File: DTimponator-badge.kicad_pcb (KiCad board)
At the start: 2 copper layers, 71 x 99.5 mm, 29 parts, among them J1 AVR-ISP, SW1 SW_SPDT, SW2 SW_Push, SW3 SW_Push, U1 ATtiny84A-PU

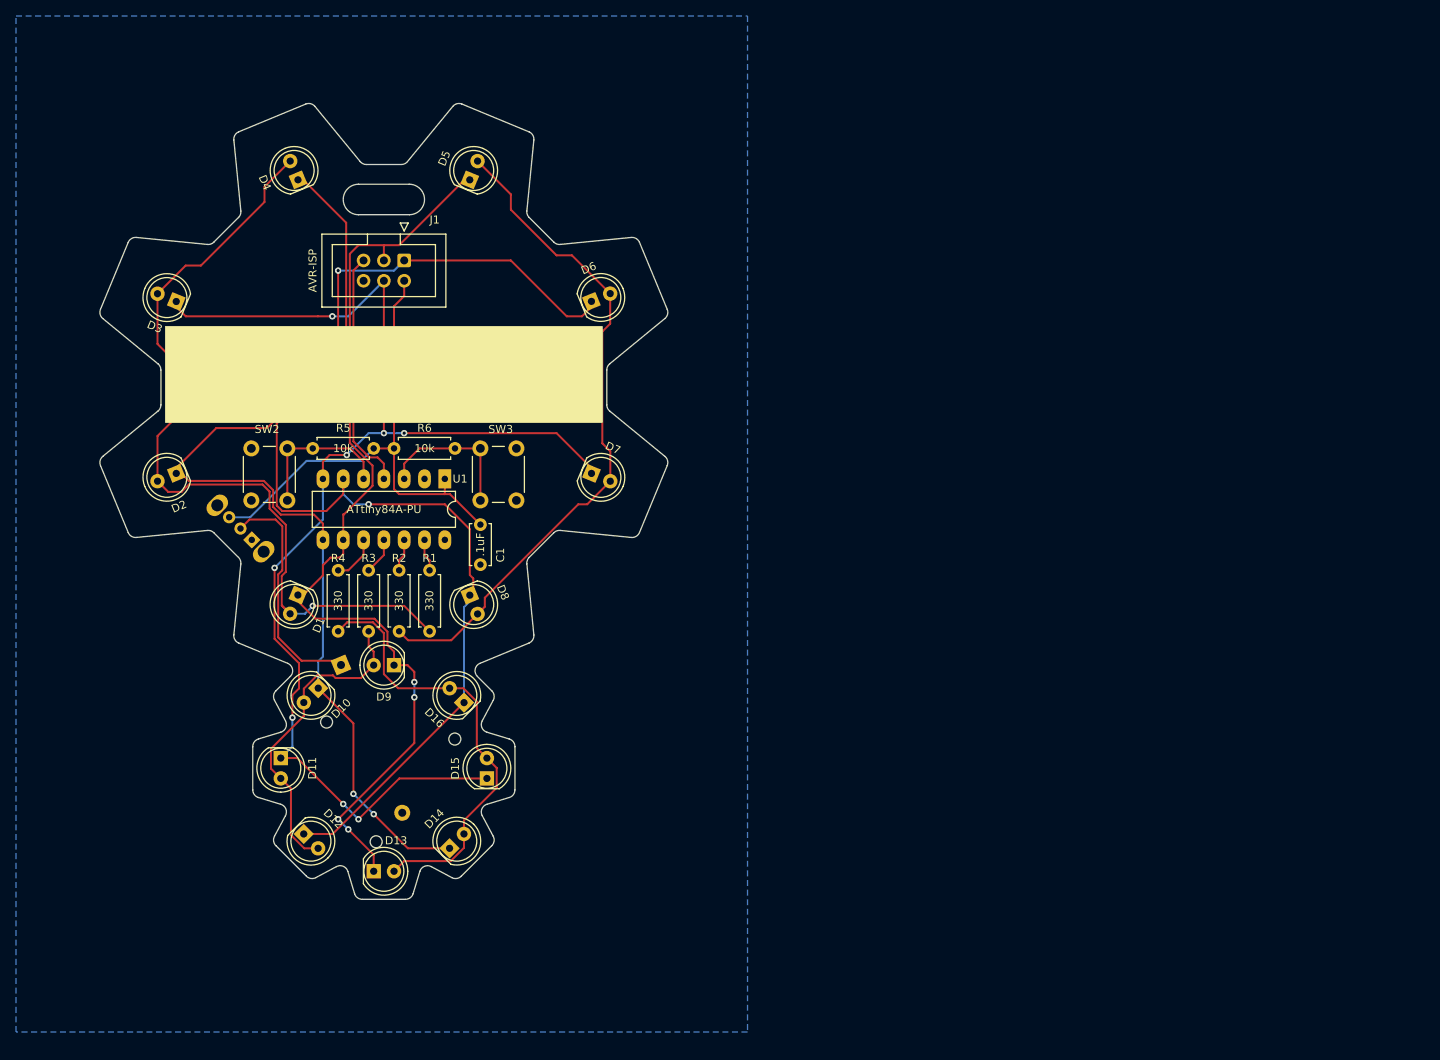
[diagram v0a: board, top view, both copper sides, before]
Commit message: Changed to dimmable SMD LEDs
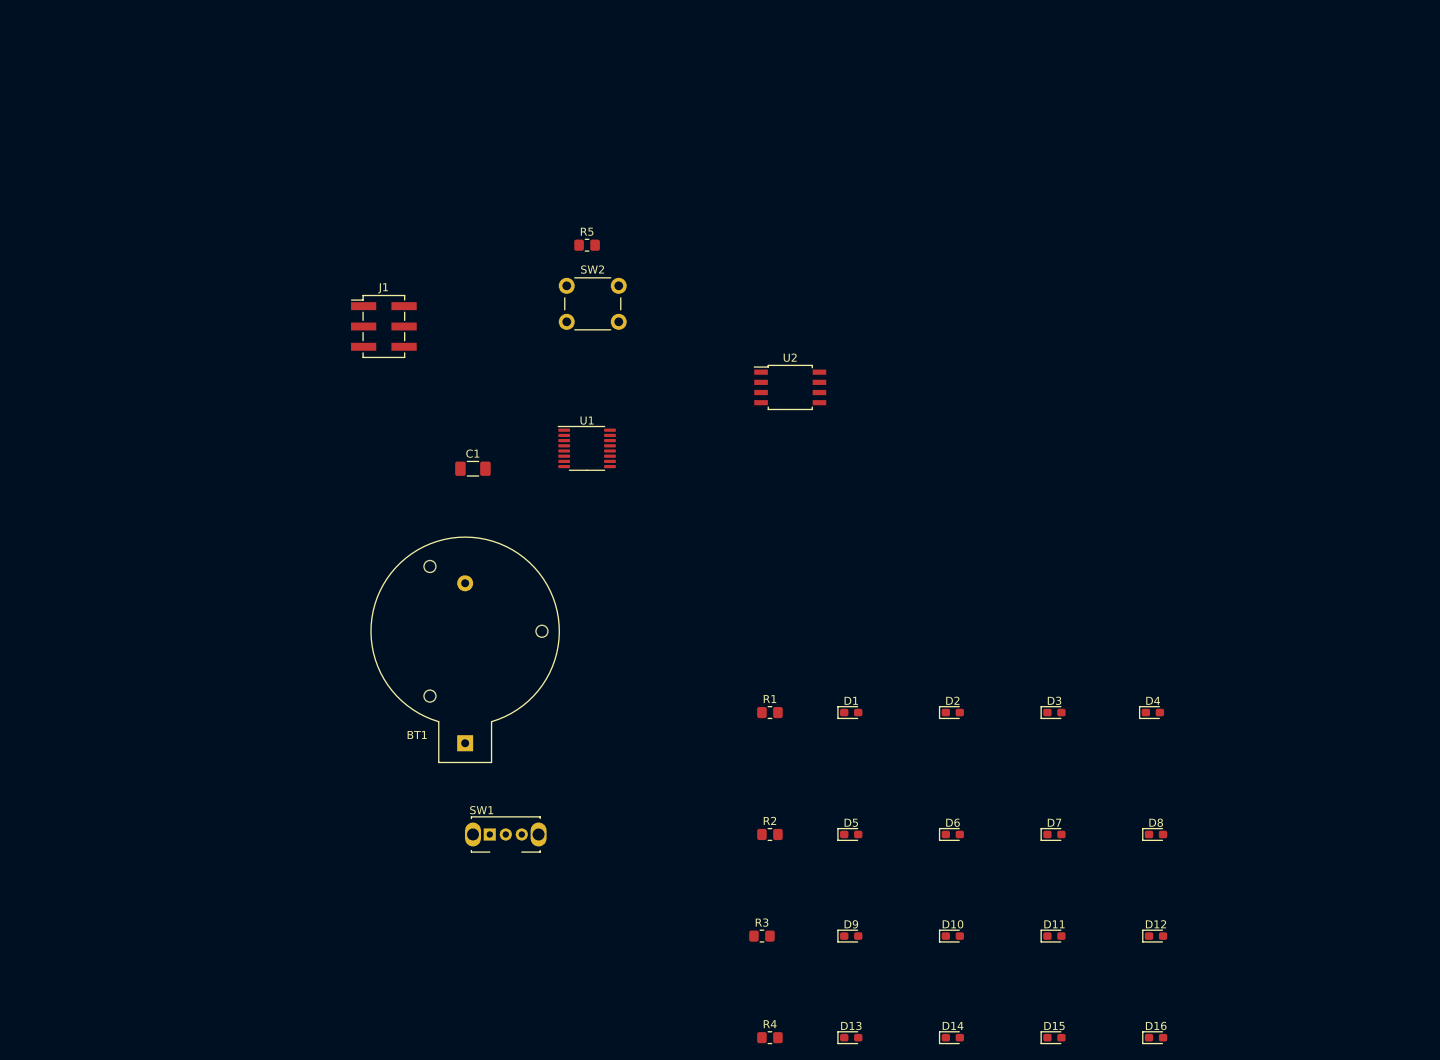
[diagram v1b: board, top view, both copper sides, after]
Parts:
- removed R6: 10k, Resistor_THT:R_Axial_DIN0207_L6.3mm_D2.5mm_P7.62mm_Horizontal
- removed SW3: SW_Push, Button_Switch_THT:SW_PUSH_6mm_H5mm
- added U2: ATtiny85-20S, Package_SO:SOIC-8W_5.3x5.3mm_P1.27mm, F.Cu at (127.0, 76.2)
- BT1: footprint CogLightBadgeTHT:MP000362_CR2032_Holder_THT -> DTimponator-badge:MP000362_CR2032_Holder_THT; moved to F.Cu
- C1: footprint Capacitor_THT:C_Disc_D5.0mm_W2.5mm_P5.00mm -> Capacitor_SMD:C_1206_3216Metric_Pad1.33x1.80mm_HandSolder
- D1, D10, D11, D12, D13, D14, D15, D16, D2, D3, D4, D5, D6, D7, D8, D9: footprint LED_THT:LED_D5.0mm -> LED_SMD:LED_0603_1608Metric_Pad1.05x0.95mm_HandSolder
- J1: footprint Connector_IDC:IDC-Header_2x03_P2.54mm_Vertical -> Connector_PinHeader_2.54mm:PinHeader_2x03_P2.54mm_Vertical_SMD
- R1, R2, R3, R4: value 330 -> R; footprint Resistor_THT:R_Axial_DIN0207_L6.3mm_D2.5mm_P7.62mm_Horizontal -> Resistor_SMD:R_0805_2012Metric_Pad1.20x1.40mm_HandSolder
- R5: footprint Resistor_THT:R_Axial_DIN0207_L6.3mm_D2.5mm_P7.62mm_Horizontal -> Resistor_SMD:R_0805_2012Metric_Pad1.20x1.40mm_HandSolder
- SW1: footprint CogLightBadgeTHT:OS102011MA1QN1_SPDT_SlideSwithch_THT -> DTimponator-badge:OS102011MA1QN1_SPDT_SlideSwithch_THT; moved to F.Cu
- U1: value ATtiny84A-PU -> 74HC595; footprint Package_DIP:DIP-14_W7.62mm_LongPads -> Package_SO:TSSOP-16_4.4x5mm_P0.65mm
- moved D4 125.9 mm to (172.3, 116.8), turned to 0 degrees
- moved D3 121.2 mm to (160.0, 116.8), turned to 0 degrees
- moved D12 107.3 mm to (172.7, 144.8), turned to 0 degrees
- moved D2 101.6 mm to (147.3, 116.8), turned to 0 degrees
- moved D11 99.2 mm to (160.0, 144.8), turned to 0 degrees
- moved D16 96.1 mm to (172.7, 157.5), turned to 0 degrees
- moved D5 94.7 mm to (134.6, 132.1), turned to 0 degrees
- moved D8 90.8 mm to (172.7, 132.1), turned to 0 degrees
- moved D10 85.2 mm to (147.3, 144.8), turned to 0 degrees
- moved D6 80.5 mm to (147.3, 132.1), turned to 0 degrees
- moved D15 78.0 mm to (160.0, 157.5), turned to 0 degrees
- moved R4 74.1 mm to (124.5, 157.5), turned to 0 degrees
- moved D7 73.4 mm to (160.0, 132.1), turned to 0 degrees
- moved D1 70.7 mm to (134.6, 116.8), turned to 0 degrees
- moved D14 67.2 mm to (147.3, 157.5), turned to 0 degrees
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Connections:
- D1 pad 1: /sink1 -> Net-(D1-Pad1)
- D10 pad 1: /sink2 -> Net-(D10-Pad1)
- D11 pad 1: /sink3 -> Net-(D10-Pad1)
- D11 pad 2: Net-(D10-Pad2) -> Net-(D11-Pad2)
- D12 pad 1: /sink4 -> Net-(D10-Pad1)
- D12 pad 2: Net-(D10-Pad2) -> Net-(D12-Pad2)
- D13 pad 1: /sink1 -> Net-(D13-Pad1)
- D13 pad 2: Net-(D13-Pad2) -> Net-(D1-Pad2)
- D14 pad 1: /sink2 -> Net-(D13-Pad1)
- D14 pad 2: Net-(D13-Pad2) -> Net-(D10-Pad2)
- D15 pad 1: /sink3 -> Net-(D13-Pad1)
- D15 pad 2: Net-(D13-Pad2) -> Net-(D11-Pad2)
- D16 pad 1: /sink4 -> Net-(D13-Pad1)
- D16 pad 2: Net-(D13-Pad2) -> Net-(D12-Pad2)
- D2 pad 1: /sink2 -> Net-(D1-Pad1)
- D2 pad 2: Net-(D1-Pad2) -> Net-(D10-Pad2)
- D3 pad 1: /sink3 -> Net-(D1-Pad1)
- D3 pad 2: Net-(D1-Pad2) -> Net-(D11-Pad2)
- D4 pad 1: /sink4 -> Net-(D1-Pad1)
- D4 pad 2: Net-(D1-Pad2) -> Net-(D12-Pad2)
- D5 pad 1: /sink1 -> Net-(D5-Pad1)
- D5 pad 2: Net-(D5-Pad2) -> Net-(D1-Pad2)
- D6 pad 1: /sink2 -> Net-(D5-Pad1)
- D6 pad 2: Net-(D5-Pad2) -> Net-(D10-Pad2)
- D7 pad 1: /sink3 -> Net-(D5-Pad1)
- D7 pad 2: Net-(D5-Pad2) -> Net-(D11-Pad2)
- D8 pad 1: /sink4 -> Net-(D5-Pad1)
- D8 pad 2: Net-(D5-Pad2) -> Net-(D12-Pad2)
- D9 pad 1: /sink1 -> Net-(D10-Pad1)
- D9 pad 2: Net-(D10-Pad2) -> Net-(D1-Pad2)
- J1 pad 1: /sink2 -> /MISO
- J1 pad 3: /sink1 -> /SCK
- J1 pad 4: /sink3 -> /MOSI
- J1 pad 5: Net-(J1-Pad5) -> /~{RST}
- R1 pad 1: Net-(D1-Pad2) -> Net-(D1-Pad1)
- R1 pad 2: /source1 -> Net-(R1-Pad2)
- R2 pad 1: Net-(D5-Pad2) -> Net-(D5-Pad1)
- R2 pad 2: /source2 -> Net-(R2-Pad2)
- R3 pad 1: Net-(D10-Pad2) -> Net-(D10-Pad1)
- R3 pad 2: /source3 -> Net-(R3-Pad2)
- R4 pad 1: Net-(D13-Pad2) -> Net-(D13-Pad1)
- R4 pad 2: /source4 -> Net-(R4-Pad2)
- R5 pad 2: Net-(R5-Pad2) -> /MOSI
- SW1 pad 1: Net-(SW1-Pad1) -> unconnected-(SW1-Pad1)
- SW2 pad 1: Net-(R5-Pad2) -> /MOSI
- U1 pad 1: VCC -> Net-(D1-Pad1)
- U1 pad 10: /source4 -> VCC
- U1 pad 11: /source3 -> /SCK
- U1 pad 12: /source2 -> /MISO
- U1 pad 13: /source1 -> /~{OE}_PWM
- U1 pad 14: GND -> /SER
- U1 pad 2: Net-(U1-Pad2) -> Net-(D1-Pad1)
- U1 pad 3: Net-(R6-Pad2) -> Net-(D1-Pad1)
- U1 pad 4: Net-(J1-Pad5) -> Net-(R1-Pad2)
- U1 pad 5: Net-(R5-Pad2) -> Net-(R2-Pad2)
- U1 pad 6: /sink4 -> Net-(R3-Pad2)
- U1 pad 7: /sink3 -> Net-(R4-Pad2)
- U1 pad 8: /sink2 -> GND
- U1 pad 9: /sink1 -> unconnected-(U1-Pad9)
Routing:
- net /sink3: track 160.6 -> 0.00 mm, vias 8 -> 0
- net /sink2: track 146.6 -> 0.00 mm, vias 3 -> 0
- net /sink4: track 127.3 -> 0.00 mm, vias 1 -> 0
- net /sink1: track 121.2 -> 0.00 mm, vias 4 -> 0
- net Net-(D1-Pad2): track 102.0 -> 0.00 mm, vias 1 -> 0
- net Net-(D5-Pad2): track 84.6 -> 0.00 mm
- net VCC: track 65.3 -> 0.00 mm
- net Net-(D13-Pad2): track 55.9 -> 0.00 mm
- net Net-(D10-Pad2): track 39.8 -> 0.00 mm
- net Net-(J1-Pad5): track 30.0 -> 0.00 mm
- net Net-(BT1-Pad1): track 29.4 -> 0.00 mm
- net Net-(R5-Pad2): track 18.9 -> 0.00 mm
- net Net-(R6-Pad2): track 18.7 -> 0.00 mm
- net /source4: track 5.87 -> 0.00 mm
- net /source3: track 4.60 -> 0.00 mm
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- removed copper zone on B.Cu, net GND
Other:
- board outline removed
- net class Default removed

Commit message: Changed from led matrix to led array for increased brightness, routed pcb.
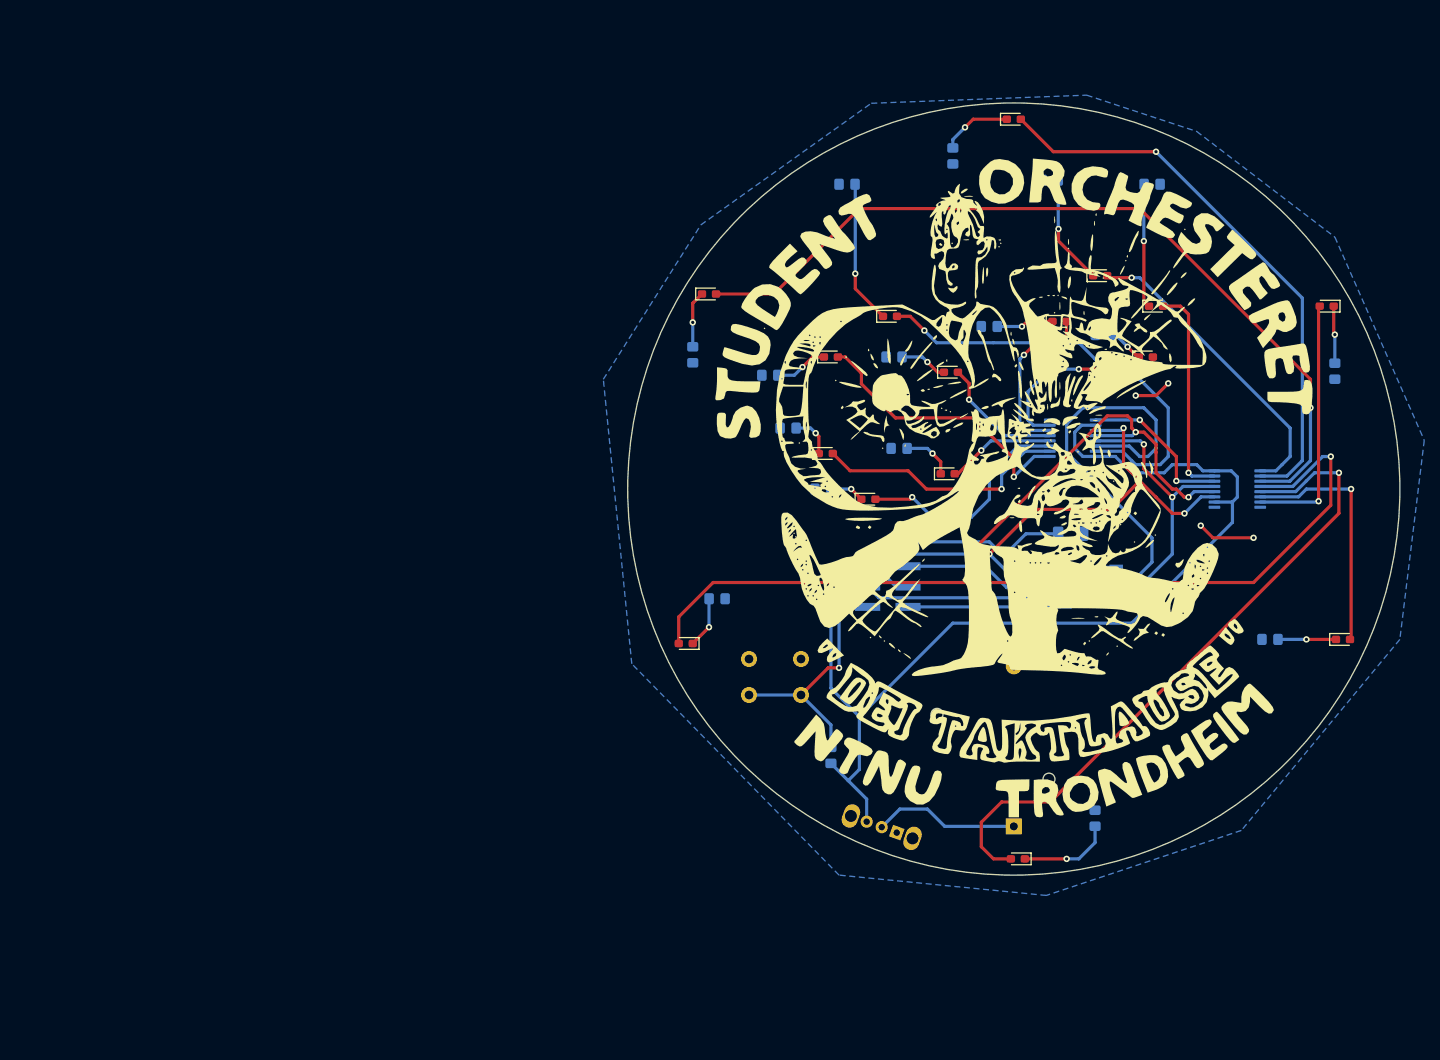
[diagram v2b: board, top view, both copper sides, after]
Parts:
- removed C1: .1uF, Capacitor_SMD:C_1206_3216Metric_Pad1.33x1.80mm_HandSolder
- added C1, 1uF: .1uF, Capacitor_SMD:C_1206_3216Metric_Pad1.33x1.80mm_HandSolder, B.Cu at (162.1, 94.5)
- added G***: LOGO, DTimponator-badge:LOGO, F.Cu at (154.9, 88.9)
- added R10: 220, Resistor_SMD:R_0805_2012Metric_Pad1.20x1.40mm_HandSolder, B.Cu at (172.2, 50.8)
- added R11: 220, Resistor_SMD:R_0805_2012Metric_Pad1.20x1.40mm_HandSolder, B.Cu at (159.5, 50.3)
- added R12: 220, Resistor_SMD:R_0805_2012Metric_Pad1.20x1.40mm_HandSolder, B.Cu at (147.3, 47.3)
- added R13: 220, Resistor_SMD:R_0805_2012Metric_Pad1.20x1.40mm_HandSolder, B.Cu at (114.8, 72.1)
- added R14: 220, Resistor_SMD:R_0805_2012Metric_Pad1.20x1.40mm_HandSolder, B.Cu at (117.9, 102.6)
- added R15: 220, Resistor_SMD:R_0805_2012Metric_Pad1.20x1.40mm_HandSolder, B.Cu at (165.1, 130.0)
- added R16: 220, Resistor_SMD:R_0805_2012Metric_Pad1.20x1.40mm_HandSolder, B.Cu at (187.0, 107.7)
- added R17: 220, Resistor_SMD:R_0805_2012Metric_Pad1.20x1.40mm_HandSolder, B.Cu at (195.1, 74.2)
- added R6: 220, Resistor_SMD:R_0805_2012Metric_Pad1.20x1.40mm_HandSolder, B.Cu at (140.0, 72.4)
- added R7: 220, Resistor_SMD:R_0805_2012Metric_Pad1.20x1.40mm_HandSolder, B.Cu at (151.9, 68.6)
- added R8: 220, Resistor_SMD:R_0805_2012Metric_Pad1.20x1.40mm_HandSolder, B.Cu at (166.1, 69.6)
- added R9, 10k: 10k, Resistor_SMD:R_0805_2012Metric_Pad1.20x1.40mm_HandSolder, B.Cu at (132.1, 122.2)
- added U3: 74HC595, Package_SO:TSSOP-16_4.4x5mm_P0.65mm, B.Cu at (182.9, 88.9)
- BT1, J1, SW1, SW2, U1, U2: moved to B.Cu
- R1, R2, R3, R4: value R -> 220; moved to B.Cu
- R5: value 10k -> 220; moved to B.Cu
- moved D11 102.2 mm to (154.9, 42.7)
- moved D12 97.8 mm to (116.8, 64.5)
- moved D16 93.9 mm to (194.1, 66.0), turned to 180 degrees
- moved D9 87.5 mm to (172.7, 66.0)
- moved D10 84.6 mm to (165.7, 62.2)
- moved J1 70.9 mm to (139.2, 101.1), turned to 180 degrees
- moved BT1 69.4 mm to (154.9, 117.1), turned to 180 degrees
- moved R4 68.9 mm to (131.1, 88.9), turned to 180 degrees
- moved R1 66.7 mm to (134.1, 50.8), turned to 180 degrees
- moved D7 64.1 mm to (160.7, 67.9)
- moved R3 63.6 mm to (126.7, 81.3), turned to 180 degrees
- moved D15 61.5 mm to (196.1, 107.7)
- moved U1 60.7 mm to (162.3, 82.5)
- moved D8 59.7 mm to (171.4, 72.4)
- moved D6 57.8 mm to (147.1, 74.3)
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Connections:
- D11 pad 1: Net-(D10-Pad1) -> Net-(D11-Pad1)
- D12 pad 1: Net-(D10-Pad1) -> Net-(D12-Pad1)
- D13 pad 2: Net-(D1-Pad2) -> Net-(D13-Pad2)
- D14 pad 1: Net-(D13-Pad1) -> Net-(D14-Pad1)
- D14 pad 2: Net-(D10-Pad2) -> Net-(D14-Pad2)
- D15 pad 1: Net-(D13-Pad1) -> Net-(D15-Pad1)
- D15 pad 2: Net-(D11-Pad2) -> Net-(D15-Pad2)
- D16 pad 1: Net-(D13-Pad1) -> Net-(D16-Pad1)
- D16 pad 2: Net-(D12-Pad2) -> Net-(D16-Pad2)
- D2 pad 1: Net-(D1-Pad1) -> Net-(D2-Pad1)
- D2 pad 2: Net-(D10-Pad2) -> Net-(D2-Pad2)
- D3 pad 1: Net-(D1-Pad1) -> Net-(D3-Pad1)
- D3 pad 2: Net-(D11-Pad2) -> Net-(D3-Pad2)
- D4 pad 1: Net-(D1-Pad1) -> Net-(D4-Pad1)
- D4 pad 2: Net-(D12-Pad2) -> Net-(D4-Pad2)
- D5 pad 2: Net-(D1-Pad2) -> Net-(D5-Pad2)
- D6 pad 1: Net-(D5-Pad1) -> Net-(D6-Pad1)
- D6 pad 2: Net-(D10-Pad2) -> Net-(D6-Pad2)
- D7 pad 1: Net-(D5-Pad1) -> Net-(D7-Pad1)
- D7 pad 2: Net-(D11-Pad2) -> Net-(D7-Pad2)
- D8 pad 1: Net-(D5-Pad1) -> Net-(D8-Pad1)
- D8 pad 2: Net-(D12-Pad2) -> Net-(D8-Pad2)
- D9 pad 1: Net-(D10-Pad1) -> Net-(D9-Pad1)
- D9 pad 2: Net-(D1-Pad2) -> Net-(D9-Pad2)
- R1 pad 2: Net-(R1-Pad2) -> GND
- R2 pad 1: Net-(D5-Pad1) -> Net-(D2-Pad1)
- R2 pad 2: Net-(R2-Pad2) -> GND
- R3 pad 1: Net-(D10-Pad1) -> Net-(D3-Pad1)
- R3 pad 2: Net-(R3-Pad2) -> GND
- R4 pad 1: Net-(D13-Pad1) -> Net-(D4-Pad1)
- R4 pad 2: Net-(R4-Pad2) -> GND
- R5 pad 1: VCC -> Net-(D5-Pad1)
- R5 pad 2: /MOSI -> GND
- U1 pad 1: Net-(D1-Pad1) -> Net-(D2-Pad2)
- U1 pad 2: Net-(D1-Pad1) -> Net-(D3-Pad2)
- U1 pad 3: Net-(D1-Pad1) -> Net-(D4-Pad2)
- U1 pad 4: Net-(R1-Pad2) -> Net-(D5-Pad2)
- U1 pad 5: Net-(R2-Pad2) -> Net-(D6-Pad2)
- U1 pad 6: Net-(R3-Pad2) -> Net-(D7-Pad2)
- U1 pad 7: Net-(R4-Pad2) -> Net-(D8-Pad2)
- U1 pad 9: unconnected-(U1-Pad9) -> Net-(U1-Pad9)
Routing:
- net VCC: track 0.00 -> 168.5 mm
- net Net-(D13-Pad2): track 0.00 -> 107.1 mm, vias 0 -> 1
- net Net-(D12-Pad2): track 0.00 -> 105.1 mm, vias 0 -> 1
- net Net-(D14-Pad2): track 0.00 -> 84.0 mm, vias 0 -> 1
- net /SCK: track 0.00 -> 73.7 mm, vias 0 -> 3
- net /MISO: track 0.00 -> 71.5 mm, vias 0 -> 3
- net Net-(D11-Pad2): track 0.00 -> 70.8 mm, vias 0 -> 1
- net /MOSI: track 0.00 -> 58.2 mm, vias 0 -> 1
- net Net-(D1-Pad2): track 0.00 -> 54.9 mm, vias 0 -> 1
- net /SER: track 0.00 -> 51.7 mm
- net Net-(D10-Pad2): track 0.00 -> 38.8 mm, vias 0 -> 1
- net /~{OE}_PWM: track 0.00 -> 36.0 mm, vias 0 -> 2
- net Net-(D2-Pad2): track 0.00 -> 35.9 mm, vias 0 -> 1
- net Net-(D3-Pad2): track 0.00 -> 32.0 mm, vias 0 -> 1
- net Net-(D16-Pad2): track 0.00 -> 31.8 mm, vias 0 -> 1
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- added copper zone on B.Cu, net GND
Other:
- board outline added: 96.5 x 96.5 mm
- board text added: "Buttonnålfestefelt"
